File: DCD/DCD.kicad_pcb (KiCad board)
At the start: 4 copper layers, 110 x 110 mm, 141 parts, among them IC1 830S21AMI-01LF, IC2 830S21AMI-01LF, J1 UMPS-04-03.5-G-VT-SM-WT, J2 UMPS-04-03.5-G-VT-SM-WT, J3 UMPS-04-03.5-G-VT-SM-WT, J4 UMPS-04-03.5-G-VT-SM-WT, J5 Conn_01x02_Pin, U1 TLV76780DBVR, U10 OPA277UA, U11 DAC8811ICDGKT, U12 DAC8811ICDGKT, U13 OPA277UA, U14 OPA277UA, U15 MC100EP31DTG, U16 MC100EP31DTG, U2 ADP7182AUJZ-1.8-R7, U3 LP2985-50DBVR, U4 LP2985-18DBVR, U5 LP2985-33DBVR, U6 ADR4550BRZ, U7 LP2985-33DBVR, U8 CDCLVC1104PWR, U9 AD4630-24BBCZ, Y1 SiT8208AI-21-33E-50.000000

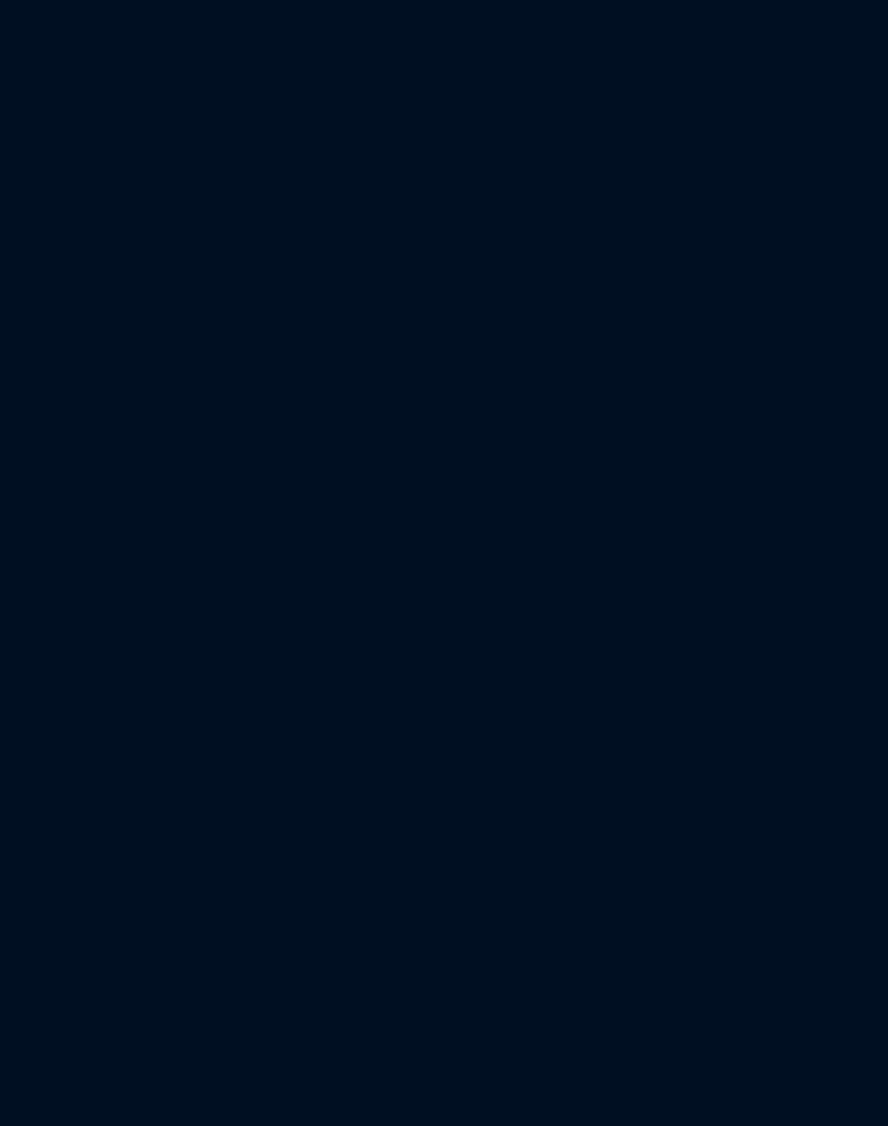
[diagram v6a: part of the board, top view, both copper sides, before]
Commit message: Added the components for the reconditioning to the pcb
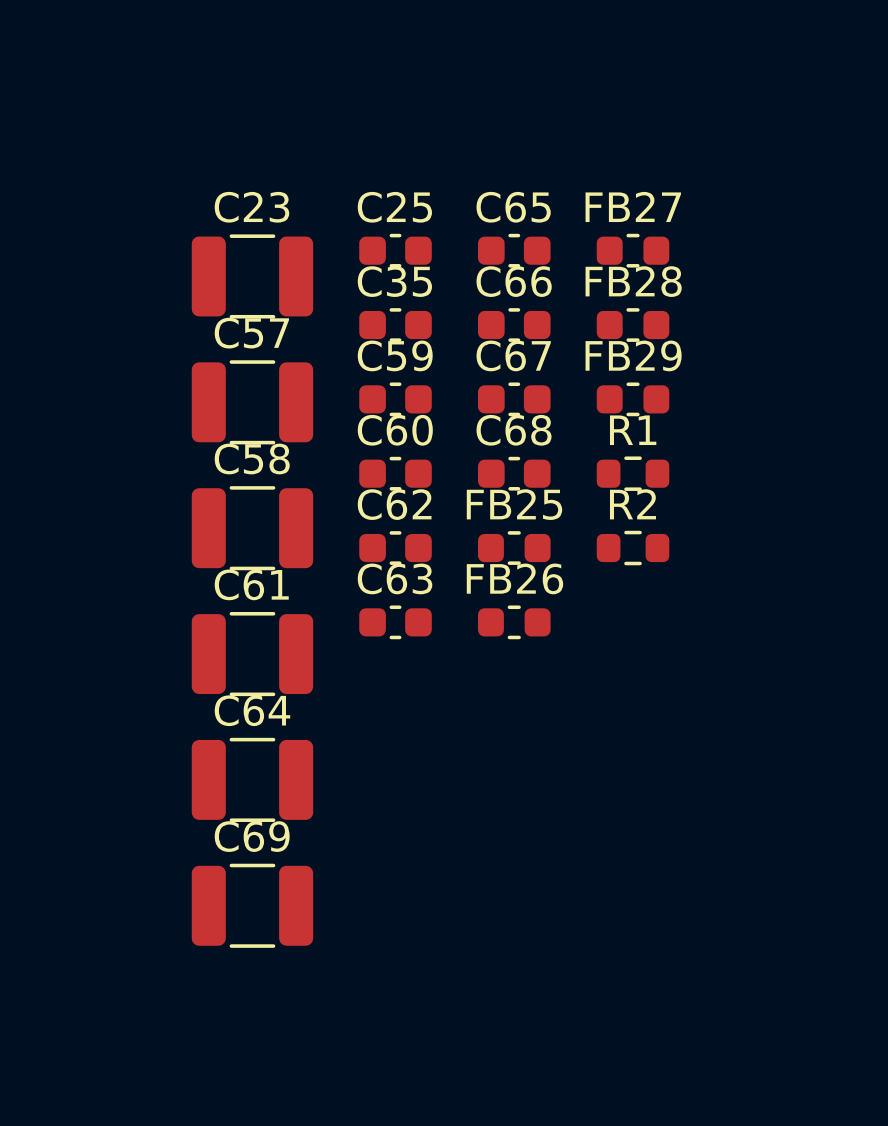
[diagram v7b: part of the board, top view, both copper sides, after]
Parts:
- added C23: 10uF, Capacitor_SMD:C_1210_3225Metric, F.Cu at (55.0, 123.0)
- added C25: 1µF, Capacitor_SMD:C_0603_1608Metric, F.Cu at (59.9, 122.1)
- added C35: 100nF, Capacitor_SMD:C_0603_1608Metric, F.Cu at (59.9, 124.6)
- added C57: 10uF, Capacitor_SMD:C_1210_3225Metric, F.Cu at (55.0, 127.2)
- added C58: 10uF, Capacitor_SMD:C_1210_3225Metric, F.Cu at (55.0, 131.5)
- added C59: 1µF, Capacitor_SMD:C_0603_1608Metric, F.Cu at (59.9, 127.2)
- added C60: 100nF, Capacitor_SMD:C_0603_1608Metric, F.Cu at (59.9, 129.7)
- added C61: 10uF, Capacitor_SMD:C_1210_3225Metric, F.Cu at (55.0, 135.8)
- added C62: 1µF, Capacitor_SMD:C_0603_1608Metric, F.Cu at (59.9, 132.2)
- added C63: 100nF, Capacitor_SMD:C_0603_1608Metric, F.Cu at (59.9, 134.7)
- added C64: 10uF, Capacitor_SMD:C_1210_3225Metric, F.Cu at (55.0, 140.0)
- added C65: 1µF, Capacitor_SMD:C_0603_1608Metric, F.Cu at (63.9, 122.1)
- added C66: 100nF, Capacitor_SMD:C_0603_1608Metric, F.Cu at (63.9, 124.6)
- added C67: 100nF, Capacitor_SMD:C_0603_1608Metric, F.Cu at (63.9, 127.2)
- added C68: 1µF, Capacitor_SMD:C_0603_1608Metric, F.Cu at (63.9, 129.7)
- added C69: 10uF, Capacitor_SMD:C_1210_3225Metric, F.Cu at (55.0, 144.2)
- added FB25: 470Ω, Inductor_SMD:L_0603_1608Metric, F.Cu at (63.9, 132.2)
- added FB26: 470Ω, Inductor_SMD:L_0603_1608Metric, F.Cu at (63.9, 134.7)
- added FB27: 470Ω, Inductor_SMD:L_0603_1608Metric, F.Cu at (67.9, 122.1)
- added FB28: 470Ω, Inductor_SMD:L_0603_1608Metric, F.Cu at (67.9, 124.6)
- added FB29: 470Ω, Inductor_SMD:L_0603_1608Metric, F.Cu at (67.9, 127.2)
- added R1: 10k, Resistor_SMD:R_0603_1608Metric, F.Cu at (67.9, 129.7)
- added R2: 10k, Resistor_SMD:R_0603_1608Metric, F.Cu at (67.9, 132.2)
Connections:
- C24 pad 1: Net-(U7-VOUT) -> 3V3_CLK
- C26 pad 1: unconnected-(C26-Pad1) -> Net-(Y1-VDD)
- C26 pad 2: Net-(C26-Pad2) -> /ADC/DGND
- C34 pad 1: unconnected-(C34-Pad1) -> Net-(Y1-VDD)
- C34 pad 2: Net-(C26-Pad2) -> /ADC/DGND
- FB21 pad 1: unconnected-(FB21-Pad1) -> 3V3_CLK
- FB21 pad 2: unconnected-(FB21-Pad2) -> Net-(Y1-VDD)
- IC1 pad 2: unconnected-(IC1-CLK-Pad2) -> Net-(IC1-CLK)
- IC1 pad 3: unconnected-(IC1-NCLK-Pad3) -> Net-(IC1-NCLK)
- IC1 pad 5: unconnected-(IC1-GND-Pad5) -> /ADC/DGND
- IC1 pad 7: unconnected-(IC1-Q-Pad7) -> /Comms/*CS
- IC1 pad 8: unconnected-(IC1-VDD-Pad8) -> Net-(IC1-VDD)
- IC2 pad 2: unconnected-(IC2-CLK-Pad2) -> Net-(IC2-CLK)
- IC2 pad 3: unconnected-(IC2-NCLK-Pad3) -> Net-(IC2-NCLK)
- IC2 pad 5: unconnected-(IC2-GND-Pad5) -> /ADC/DGND
- IC2 pad 7: unconnected-(IC2-Q-Pad7) -> /ADC/CNV
- IC2 pad 8: unconnected-(IC2-VDD-Pad8) -> Net-(IC2-VDD)
- U15 pad 2: unconnected-(U15-D-Pad2) -> /Comms/Signal Reconditioning/*CS
- U15 pad 3: unconnected-(U15-CLK-Pad3) -> CS_CLK
- U15 pad 5: unconnected-(U15-VEE-Pad5) -> /ADC/DGND
- U15 pad 6: unconnected-(U15-*Q-Pad6) -> Net-(IC1-NCLK)
- U15 pad 7: unconnected-(U15-Q-Pad7) -> Net-(IC1-CLK)
- U15 pad 8: unconnected-(U15-VCC-Pad8) -> Net-(U15-VCC)
- U16 pad 2: unconnected-(U16-D-Pad2) -> /Comms/Signal Reconditioning/CNV
- U16 pad 3: unconnected-(U16-CLK-Pad3) -> CNV_CLK
- U16 pad 5: unconnected-(U16-VEE-Pad5) -> /ADC/DGND
- U16 pad 6: unconnected-(U16-*Q-Pad6) -> Net-(IC2-NCLK)
- U16 pad 7: unconnected-(U16-Q-Pad7) -> Net-(IC2-CLK)
- U16 pad 8: unconnected-(U16-VCC-Pad8) -> Net-(U16-VCC)
- U7 pad 5: Net-(U7-VOUT) -> 3V3_CLK
- U8 pad 1: unconnected-(U8-CLKIN-Pad1) -> Net-(U8-CLKIN)
- U8 pad 2: unconnected-(U8-1G-Pad2) -> Net-(U8-1G)
- U8 pad 3: unconnected-(U8-Y0-Pad3) -> CS_CLK
- U8 pad 4: unconnected-(U8-GND-Pad4) -> /ADC/DGND
- U8 pad 5: unconnected-(U8-Y2-Pad5) -> /Comms/Signal Reconditioning/CLK
- U8 pad 6: unconnected-(U8-VDD-Pad6) -> Net-(U8-VDD)
- U8 pad 7: unconnected-(U8-Y3-Pad7) -> /Comms/CLK
- U8 pad 8: unconnected-(U8-Y1-Pad8) -> CNV_CLK
- Y1 pad 1: unconnected-(Y1-OE/~{ST}-Pad1) -> Net-(Y1-OE/~{ST})
- Y1 pad 2: unconnected-(Y1-GND-Pad2) -> /ADC/DGND
- Y1 pad 3: unconnected-(Y1-OUT-Pad3) -> Net-(U8-CLKIN)
- Y1 pad 4: unconnected-(Y1-VDD-Pad4) -> Net-(Y1-VDD)

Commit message: Progress on the layout of the signal reconditioning circuit
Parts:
- moved IC1 141.8 mm to (192.7, 107.1)
- moved U15 141.4 mm to (192.1, 112.7)
- moved C61 132.3 mm to (185.6, 114.5)
- moved C23 131.7 mm to (185.6, 106.0)
- moved C23 123.6 mm to (185.6, 110.2)
- moved C59 122.9 mm to (180.8, 105.1)
- moved C60 122.9 mm to (180.8, 107.6)
- moved C62 122.9 mm to (180.8, 110.1)
- moved C63 122.9 mm to (180.8, 112.6)
- moved FB26 118.6 mm to (180.8, 115.1)
- moved FB27 113.0 mm to (180.8, 117.6)
- moved Y1 112.2 mm to (168.7, 132.5), turned to 90 degrees
- moved FB21 110.8 mm to (163.7, 137.8), turned to 90 degrees
- moved C58 108.5 mm to (163.5, 133.0), turned to 90 degrees
- moved C34 106.8 mm to (158.7, 137.8), turned to 90 degrees
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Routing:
- net Net-(U1-OUT): track 199.9 -> 106.3 mm
- net Net-(U3-VOUT): track 70.2 -> 16.1 mm
- net /Comms/-Vin: track 181.0 -> 126.9 mm
- net /ADC/5V: track 47.3 -> 6.12 mm, vias 4 -> 0
- net Net-(FB24-Pad1): track 0.00 -> 15.1 mm
- net /ADC/SDO0: track 27.6 -> 38.8 mm
- net /DAC/3.3V: track 82.1 -> 71.9 mm, vias 0 -> 2
- net Net-(J3-Pin_3): track 14.4 -> 4.77 mm
- net /ADC/1.8V: track 46.8 -> 39.1 mm
- net /ADC/VIO: track 61.5 -> 54.4 mm, vias 2 -> 0
- net /ADC/7V: track 79.5 -> 73.1 mm
- net /Comms/+Vin: track 14.5 -> 8.15 mm
- net Net-(FB23-Pad1): track 0.00 -> 6.06 mm
- net Net-(FB22-Pad1): track 0.00 -> 5.48 mm
- net Net-(J3-Pin_4): track 8.78 -> 6.36 mm
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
